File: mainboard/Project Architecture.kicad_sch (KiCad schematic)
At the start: 0 parts

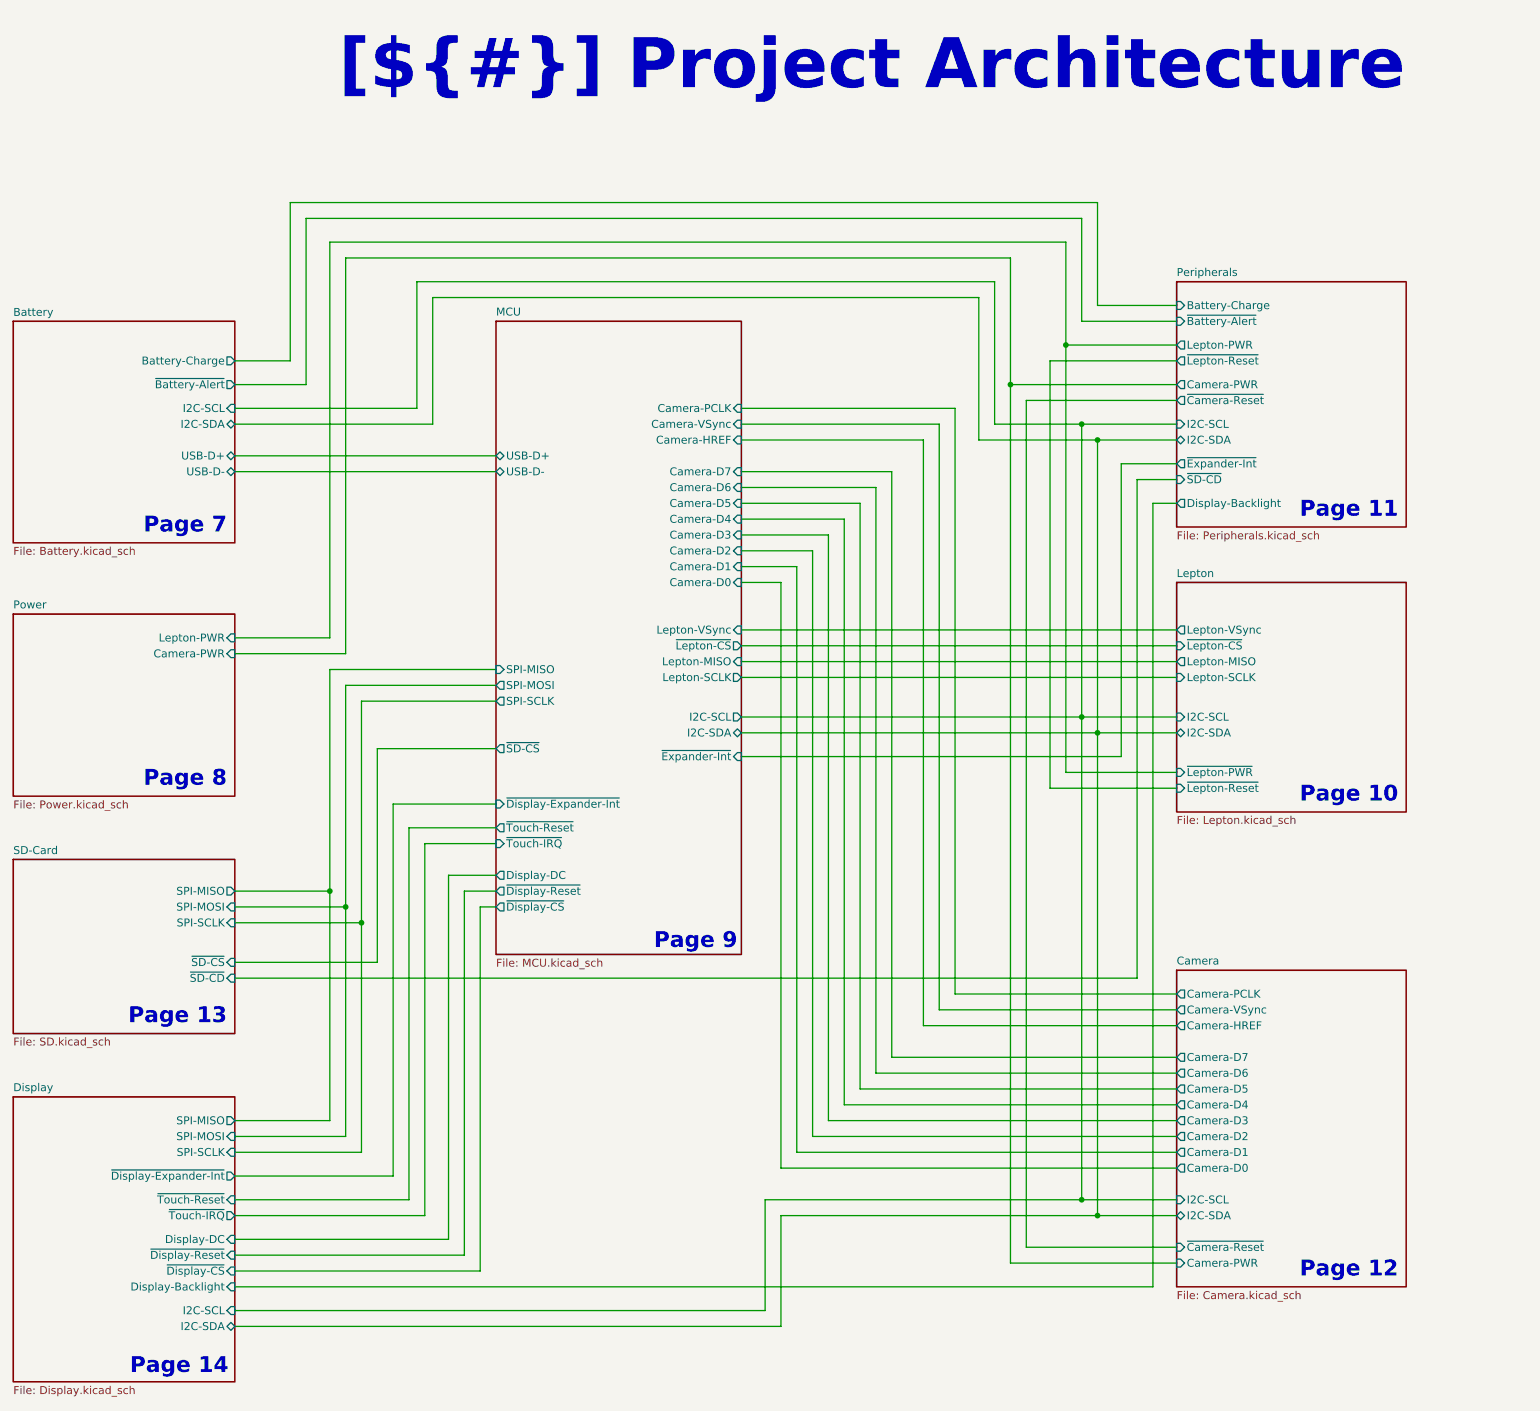
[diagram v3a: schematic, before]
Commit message: Removed: Remove camera PWD signal from camera power supply enable
- The camera PWD signal is now used as a separate signal
- Solves incompatible signal levels for both enable pins
- Fix DRC issues

Signed-off-by: Daniel Kampert <DanielKampert@kampis-elektroecke.de>
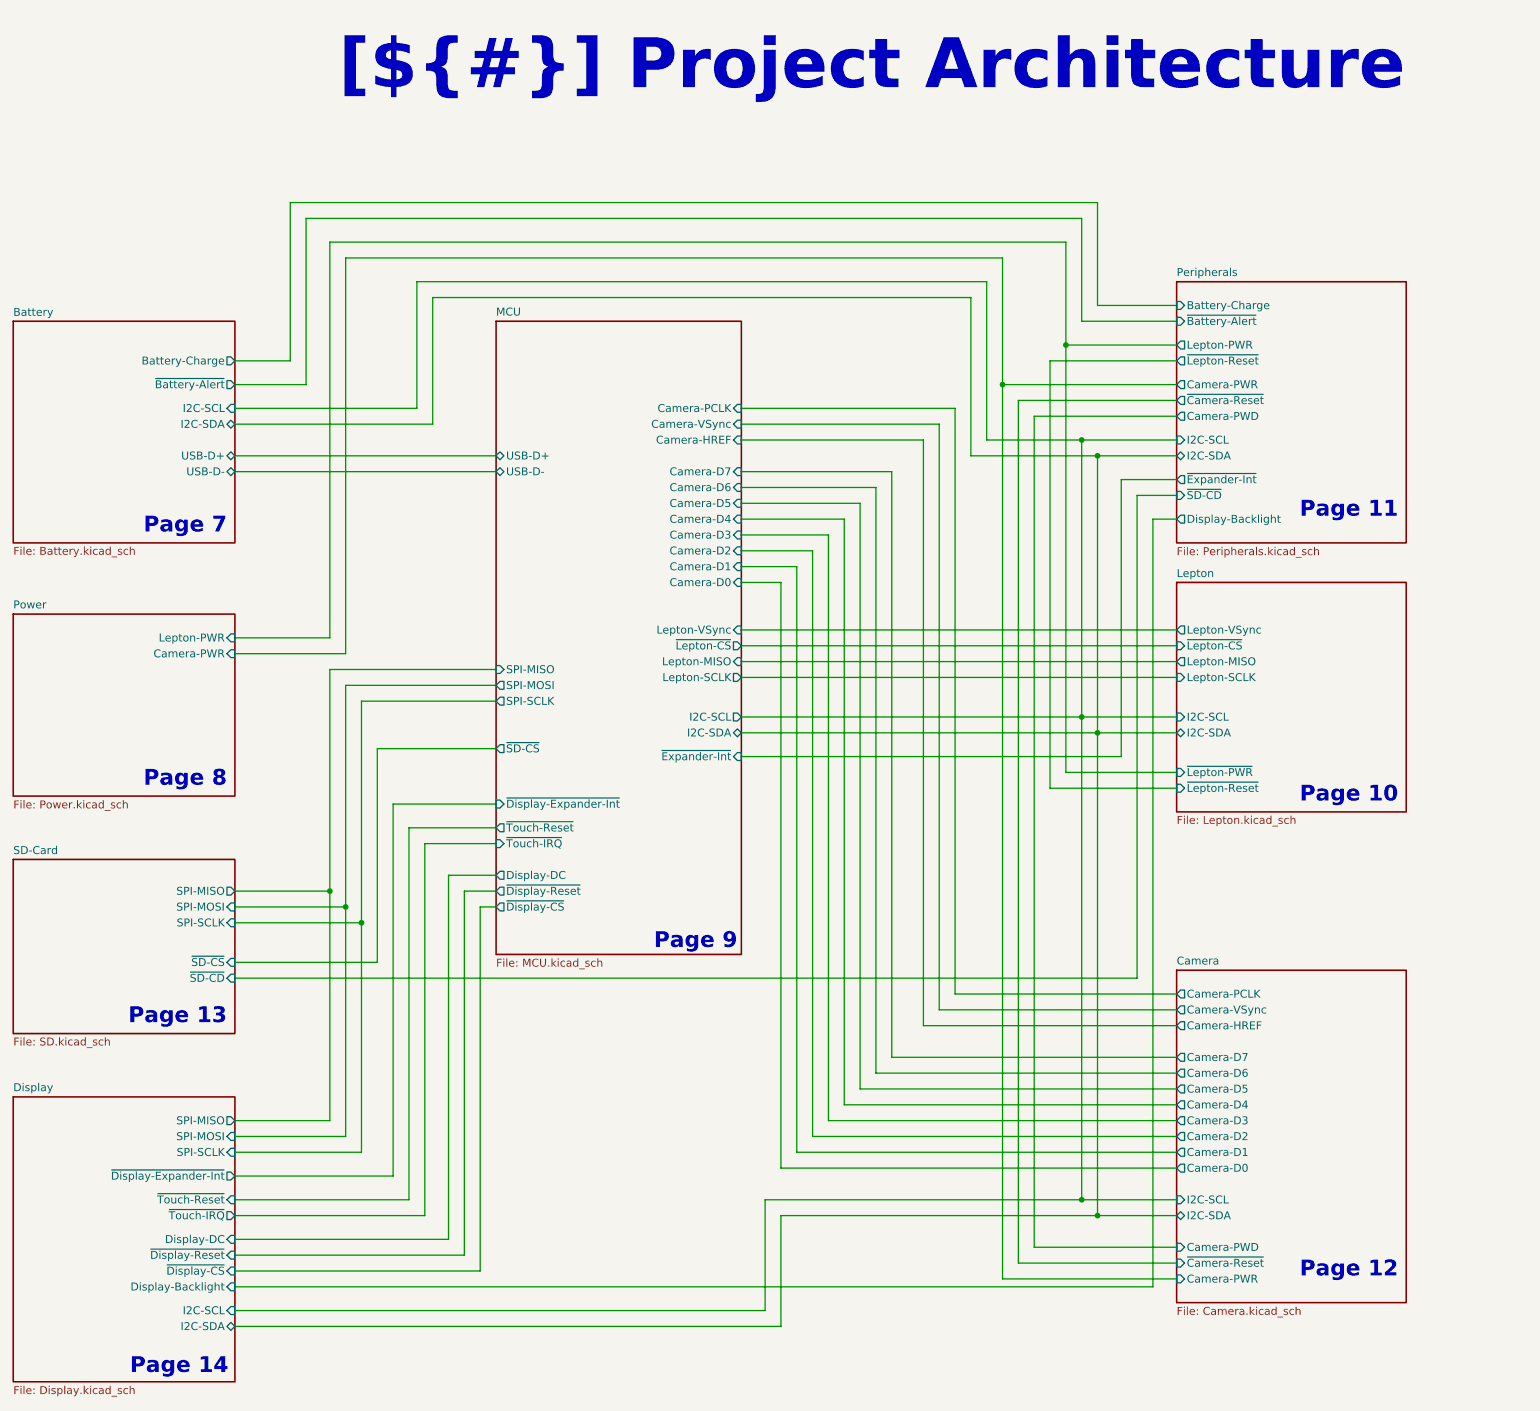
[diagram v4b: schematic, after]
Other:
- sheet Camera ports: added Camera-PWD; removed none
- sheet Peripherals ports: added Camera-PWD; removed none
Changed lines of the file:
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@@
 	)
 	(junction
-		(at 243.84 77.47)
+		(at 231.14 71.12)
 		(diameter 0)
 		(color 0 0 0 0)
@@
 	)
 	(junction
-		(at 232.41 71.12)
+		(at 246.38 82.55)
 		(diameter 0)
 		(color 0 0 0 0)
@@
 	)
 	(junction
+		(at 243.84 80.01)
+		(diameter 0)
+		(color 0 0 0 0)
+	)
+	(junction
 		(at 128.27 157.48)
 		(diameter 0)
@@
 	)
 	(junction
-		(at 246.38 80.01)
-		(diameter 0)
-		(color 0 0 0 0)
-	)
-	(junction
 		(at 243.84 124.46)
 		(diameter 0)
@@
 	(wire
 		(pts
-			(xy 259.08 86.36) (xy 252.73 86.36)
+			(xy 259.08 88.9) (xy 252.73 88.9)
 		)
 		(stroke
@@
 	(wire
 		(pts
+			(xy 259.08 209.55) (xy 236.22 209.55)
+		)
+		(stroke
+			(width 0)
+			(type default)
+		)
+	)
+	(wire
+		(pts
 			(xy 107.95 219.71) (xy 193.04 219.71)
 		)
@@
 	(wire
 		(pts
-			(xy 250.19 83.82) (xy 259.08 83.82)
+			(xy 250.19 86.36) (xy 259.08 86.36)
 		)
 		(stroke
@@
 	(wire
 		(pts
-			(xy 250.19 83.82) (xy 250.19 130.81)
-		)
-		(stroke
-			(width 0)
-			(type default)
-		)
-	)
-	(wire
-		(pts
-			(xy 246.38 80.01) (xy 259.08 80.01)
+			(xy 250.19 86.36) (xy 250.19 130.81)
+		)
+		(stroke
+			(width 0)
+			(type default)
+		)
+	)
+	(wire
+		(pts
+			(xy 246.38 82.55) (xy 259.08 82.55)
 		)
 		(stroke
@@
 	(wire
 		(pts
-			(xy 243.84 77.47) (xy 229.87 77.47)
+			(xy 243.84 80.01) (xy 228.6 80.01)
 		)
 		(stroke
@@
 	(wire
 		(pts
-			(xy 234.95 209.55) (xy 259.08 209.55)
+			(xy 233.68 212.09) (xy 259.08 212.09)
 		)
 		(stroke
@@
 	(wire
 		(pts
+			(xy 231.14 71.12) (xy 259.08 71.12)
+		)
+		(stroke
+			(width 0)
+			(type default)
+		)
+	)
+	(wire
+		(pts
 			(xy 220.98 171.45) (xy 220.98 77.47)
 		)
@@
 	(wire
 		(pts
-			(xy 252.73 86.36) (xy 252.73 166.37)
+			(xy 252.73 88.9) (xy 252.73 166.37)
 		)
 		(stroke
@@
 	(wire
 		(pts
-			(xy 259.08 90.17) (xy 255.27 90.17)
+			(xy 259.08 92.71) (xy 255.27 92.71)
 		)
 		(stroke
@@
 	(wire
 		(pts
-			(xy 232.41 71.12) (xy 259.08 71.12)
-		)
-		(stroke
-			(width 0)
-			(type default)
-		)
-	)
-	(wire
-		(pts
 			(xy 243.84 124.46) (xy 259.08 124.46)
 		)
@@
 	(wire
 		(pts
-			(xy 232.41 212.09) (xy 259.08 212.09)
+			(xy 231.14 214.63) (xy 259.08 214.63)
 		)
 		(stroke
@@
 	(wire
 		(pts
-			(xy 227.33 57.15) (xy 139.7 57.15)
+			(xy 226.06 57.15) (xy 139.7 57.15)
 		)
 		(stroke
@@
 	(wire
 		(pts
-			(xy 232.41 50.8) (xy 232.41 71.12)
+			(xy 231.14 50.8) (xy 231.14 71.12)
 		)
 		(stroke
@@
 	(wire
 		(pts
-			(xy 234.95 73.66) (xy 259.08 73.66)
+			(xy 233.68 73.66) (xy 259.08 73.66)
 		)
 		(stroke
@@
 	(wire
 		(pts
-			(xy 243.84 77.47) (xy 259.08 77.47)
+			(xy 243.84 80.01) (xy 259.08 80.01)
 		)
 		(stroke
@@
 	(wire
 		(pts
-			(xy 255.27 90.17) (xy 255.27 215.9)
+			(xy 255.27 92.71) (xy 255.27 215.9)
 		)
 		(stroke
@@
 	(wire
 		(pts
-			(xy 125.73 50.8) (xy 232.41 50.8)
+			(xy 125.73 50.8) (xy 231.14 50.8)
 		)
 		(stroke
@@
 	(wire
 		(pts
-			(xy 246.38 80.01) (xy 227.33 80.01)
+			(xy 246.38 82.55) (xy 226.06 82.55)
 		)
 		(stroke
@@
 	(wire
 		(pts
-			(xy 227.33 80.01) (xy 227.33 57.15)
+			(xy 226.06 82.55) (xy 226.06 57.15)
 		)
 		(stroke
@@
 	(wire
 		(pts
-			(xy 243.84 124.46) (xy 243.84 77.47)
-		)
-		(stroke
-			(width 0)
-			(type default)
-		)
-	)
-	(wire
-		(pts
-			(xy 229.87 77.47) (xy 229.87 54.61)
+			(xy 243.84 124.46) (xy 243.84 80.01)
+		)
+		(stroke
+			(width 0)
+			(type default)
+		)
+	)
+	(wire
+		(pts
+			(xy 228.6 80.01) (xy 228.6 54.61)
 		)
 		(stroke
@@
 	(wire
 		(pts
-			(xy 229.87 54.61) (xy 137.16 54.61)
+			(xy 228.6 54.61) (xy 137.16 54.61)
 		)
 		(stroke
@@
 	(wire
 		(pts
+			(xy 236.22 209.55) (xy 236.22 76.2)
+		)
+		(stroke
+			(width 0)
+			(type default)
+		)
+	)
+	(wire
+		(pts
 			(xy 189.23 110.49) (xy 259.08 110.49)
 		)
@@
 	(wire
 		(pts
-			(xy 234.95 209.55) (xy 234.95 73.66)
+			(xy 233.68 212.09) (xy 233.68 73.66)
 		)
 		(stroke
@@
 	(wire
 		(pts
+			(xy 236.22 76.2) (xy 259.08 76.2)
+		)
+		(stroke
+			(width 0)
+			(type default)
+		)
+	)
+	(wire
+		(pts
 			(xy 147.32 213.36) (xy 147.32 154.94)
 		)
@@
 	(wire
 		(pts
-			(xy 232.41 71.12) (xy 232.41 212.09)
+			(xy 231.14 71.12) (xy 231.14 214.63)
 		)
 		(stroke
@@
 	(wire
 		(pts
-			(xy 246.38 127) (xy 246.38 80.01)
+			(xy 246.38 127) (xy 246.38 82.55)
 		)
 		(stroke
@@
 	(sheet
 		(at 259.08 165.1)
-		(size 36.83 50.8)
+		(size 36.83 53.34)
 		(exclude_from_sim no)
 		(in_bom yes)
@@
 		)
 		(property "Sheetfile" "Camera.kicad_sch"
-			(at 259.08 216.5354 0)
+			(at 259.08 219.0754 0)
 			(effects
 				(font
@@
 		)
 		(pin "~{Camera-Reset}" input
-			(at 259.08 209.55 180)
+			(at 259.08 212.09 180)
 			(effects
 				(font
@@
 		)
 		(pin "Camera-PWR" input
-			(at 259.08 212.09 180)
+			(at 259.08 214.63 180)
 			(effects
 				(font
@@
 		(pin "I2C-SDA" bidirectional
 			(at 259.08 204.47 180)
+			(effects
+				(font
+					(size 1.27 1.27)
+				)
+				(justify left)
+			)
+		)
+		(pin "Camera-PWD" input
+			(at 259.08 209.55 180)
 			(effects
 				(font
@@
 	(sheet
 		(at 259.08 54.61)
-		(size 36.83 39.37)
+		(size 36.83 41.91)
 		(exclude_from_sim no)
 		(in_bom yes)
@@
 		)
 		(property "Sheetfile" "Peripherals.kicad_sch"
-			(at 259.08 94.6154 0)
+			(at 259.08 97.1554 0)
 			(effects
 				(font
@@
 		)
 		(pin "~{Expander-Int}" output
-			(at 259.08 83.82 180)
+			(at 259.08 86.36 180)
 			(effects
 				(font
@@
 		)
 		(pin "~{SD-CD}" input
-			(at 259.08 86.36 180)
+			(at 259.08 88.9 180)
 			(effects
 				(font
@@
 		)
 		(pin "I2C-SCL" input
-			(at 259.08 77.47 180)
+			(at 259.08 80.01 180)
 			(effects
 				(font
@@
 		)
 		(pin "I2C-SDA" bidirectional
-			(at 259.08 80.01 180)
+			(at 259.08 82.55 180)
 			(effects
 				(font
@@
 		)
 		(pin "Display-Backlight" output
-			(at 259.08 90.17 180)
+			(at 259.08 92.71 180)
 			(effects
 				(font
@@
 			(effects
 				(font
+					(size 1.27 1.27)
+				)
+				(justify left)
+			)
+		)
+		(pin "Camera-PWD" output
+			(at 259.08 76.2 180)
+			(effects
+				(font
